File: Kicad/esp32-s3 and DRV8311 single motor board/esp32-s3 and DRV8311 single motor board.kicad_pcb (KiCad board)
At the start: 4 copper layers, 38.8 x 42.1 mm, 98 parts, among them J1 JST SH SM04B, J2 7 pin FPC 0.3mm, J3 Molex_PicoBlade_53048-0310 Ho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, J4 Conn_01x02_Pin, Q3 PMOS,Si7157DP, Q4 PMOS, SW1 SW_Push, SW2 SW_Push, U1 AP2112K-3.3, U2 DRV8311HRRWR, U4 BQ25060, U5 ESP32-S3, U6 74HC595, Y1 40mhz, 10ppm

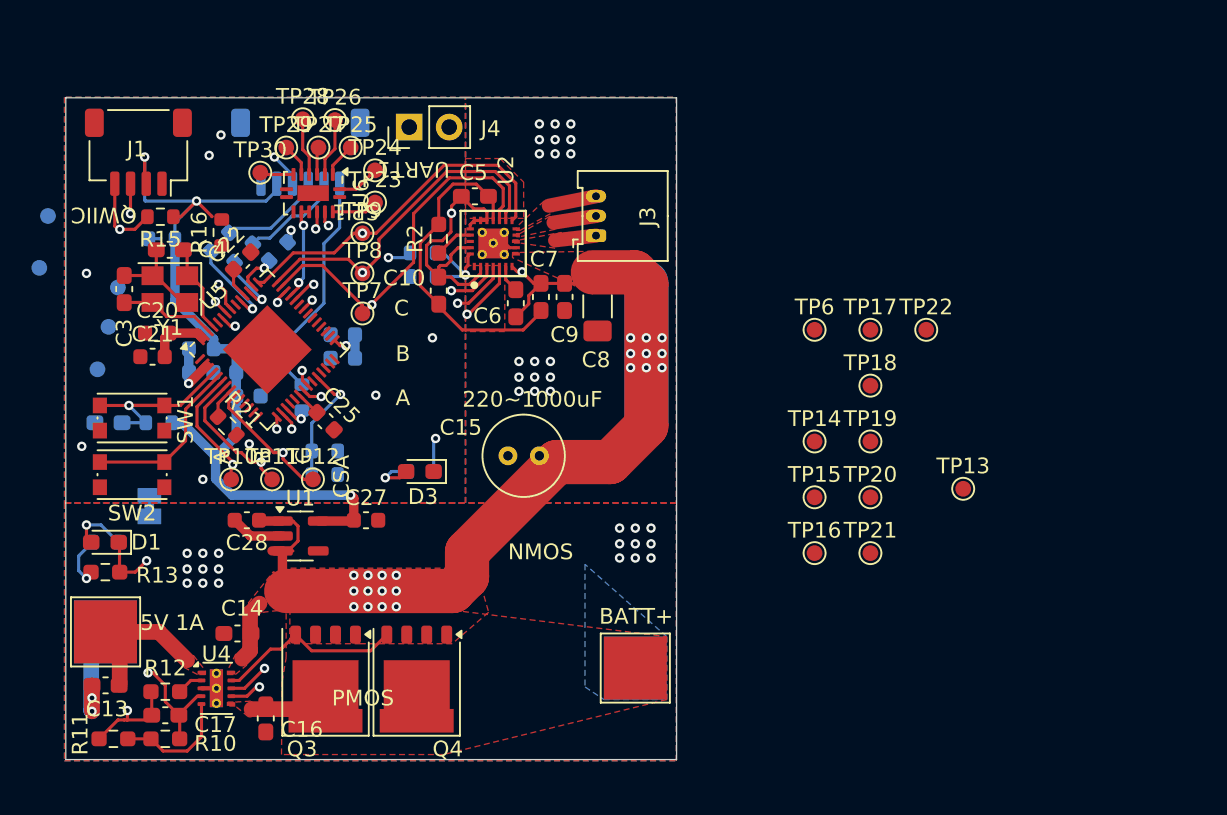
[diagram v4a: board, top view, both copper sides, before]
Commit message: Routing test pads & power
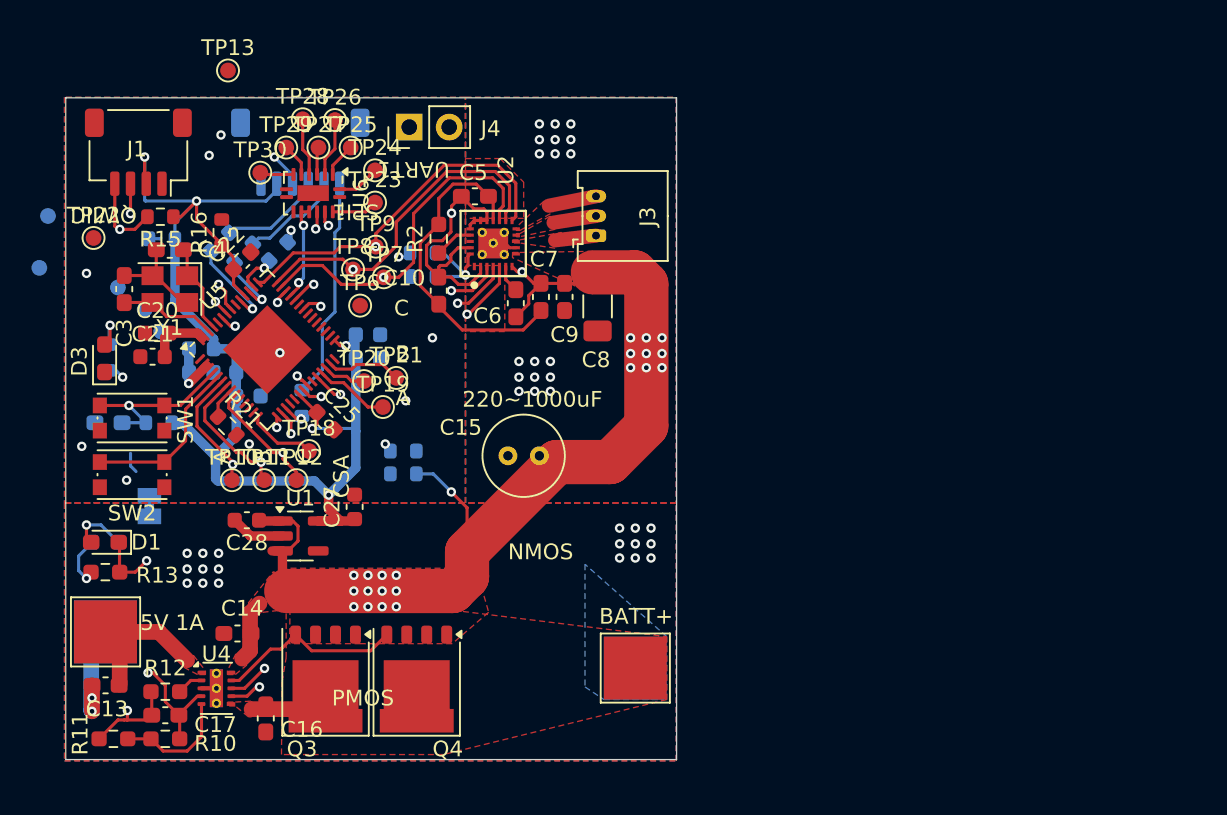
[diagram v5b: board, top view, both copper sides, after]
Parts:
- removed TP14, TP15, TP16, TP17: ~, TestPoint:TestPoint_Pad_D1.0mm
- moved TP13 53.8 mm to (133.0, 86.4)
- moved TP22 53.3 mm to (124.5, 97.0)
- moved TP18 35.9 mm to (138.2, 110.6)
- moved TP20 33.0 mm to (141.7, 106.2)
- moved TP21 32.1 mm to (143.7, 106.0)
- moved TP19 31.1 mm to (142.8, 107.8)
- moved TP6 28.9 mm to (141.4, 101.3)
- moved D3 21.3 mm to (125.2, 104.7), turned to 90 degrees
- moved R19 21.1 mm to (125.5, 104.7), turned to 90 degrees
- moved R17 5.00 mm to (144.2, 112.0)
- moved R18 5.00 mm to (144.2, 110.6)
- moved TP5 4.84 mm to (127.7, 101.6)
- moved TP1 3.36 mm to (128.8, 103.0)
- moved TP7 2.67 mm to (142.9, 99.5)
- moved C23 1.60 mm to (141.9, 103.2), turned to 0 degrees
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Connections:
- C28 pad 2: GND -> GNDPWR
- U1 pad 2: GND -> GNDPWR
- U2 pad 10: Net-(J3-Pin_3) -> Net-(J3-Pin_1)
- U2 pad 12: Net-(J3-Pin_1) -> Net-(J3-Pin_3)
- U5 pad 10: Net-(U5-GPIO5) -> unconnected-(U5-GPIO5-Pad10)
- U5 pad 11: Net-(U5-GPIO6) -> unconnected-(U5-GPIO6-Pad11)
- U5 pad 12: Net-(U5-GPIO7) -> unconnected-(U5-GPIO7-Pad12)
- U5 pad 13: Net-(U5-GPIO8) -> unconnected-(U5-GPIO8-Pad13)
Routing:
- net VDD: track 65.7 -> 83.4 mm, vias 4 -> 5
- net /MOTORPWR: track 126.1 -> 114.3 mm, vias 23 -> 24
- net /LED: track 3.19 -> 10.6 mm
- net Net-(U5-GPIO19/USB_D-): track 0.00 -> 4.83 mm
- net Net-(U5-GPIO21): track 0.00 -> 4.82 mm
- net Net-(U5-GPIO9): track 0.00 -> 4.40 mm
- net GNDPWR: track 9.07 -> 12.5 mm
- net GND: track 66.9 -> 63.5 mm, vias 10 -> 11
- net /1CSA-A: track 33.8 -> 36.9 mm
- net /1CSA-B: track 33.0 -> 35.8 mm
- net Net-(U5-GPIO20/USB_D+): track 0.00 -> 2.78 mm
- net /1CSA-C: track 30.4 -> 32.2 mm
- net unconnected-(U5-GPIO5-Pad10): track 0.00 -> 1.29 mm
- net /1C: track 29.4 -> 30.4 mm
- net /VBATT: track 7.82 -> 6.88 mm, vias 1 -> 2
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
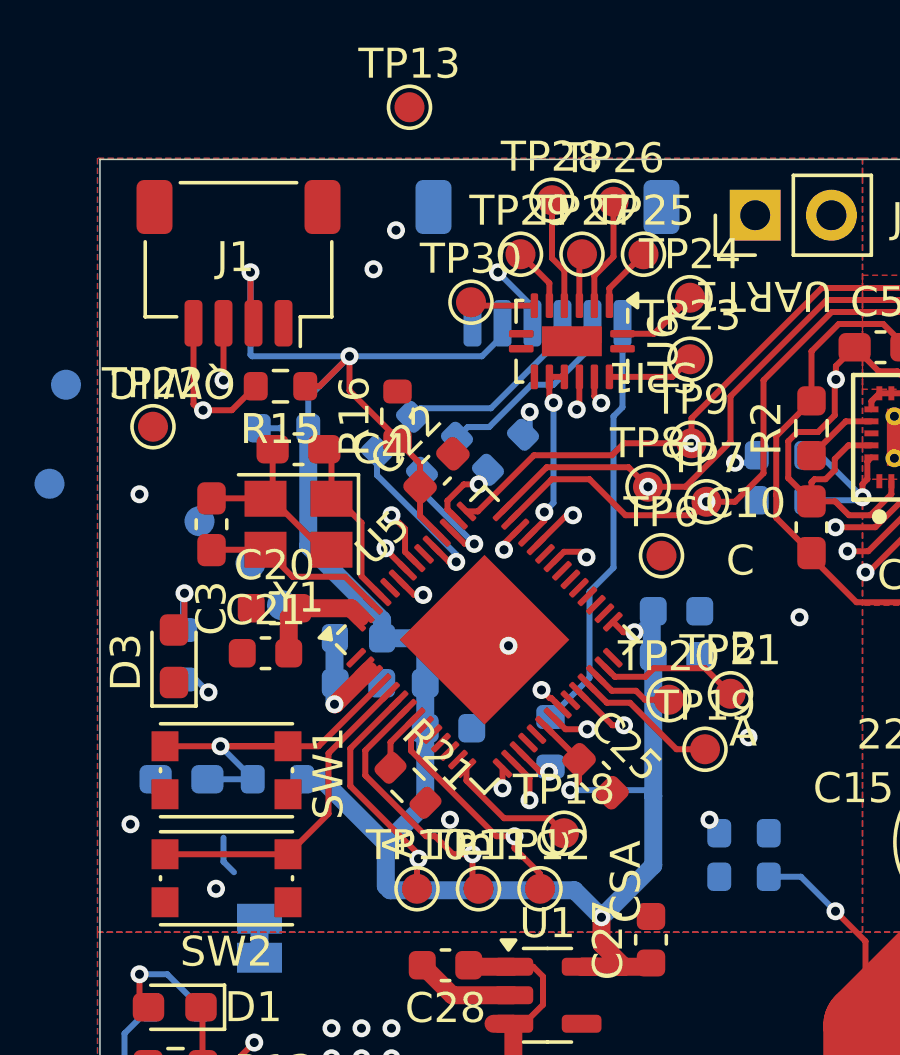
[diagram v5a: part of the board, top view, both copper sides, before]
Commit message: Added 7 pin FPC connector footprint
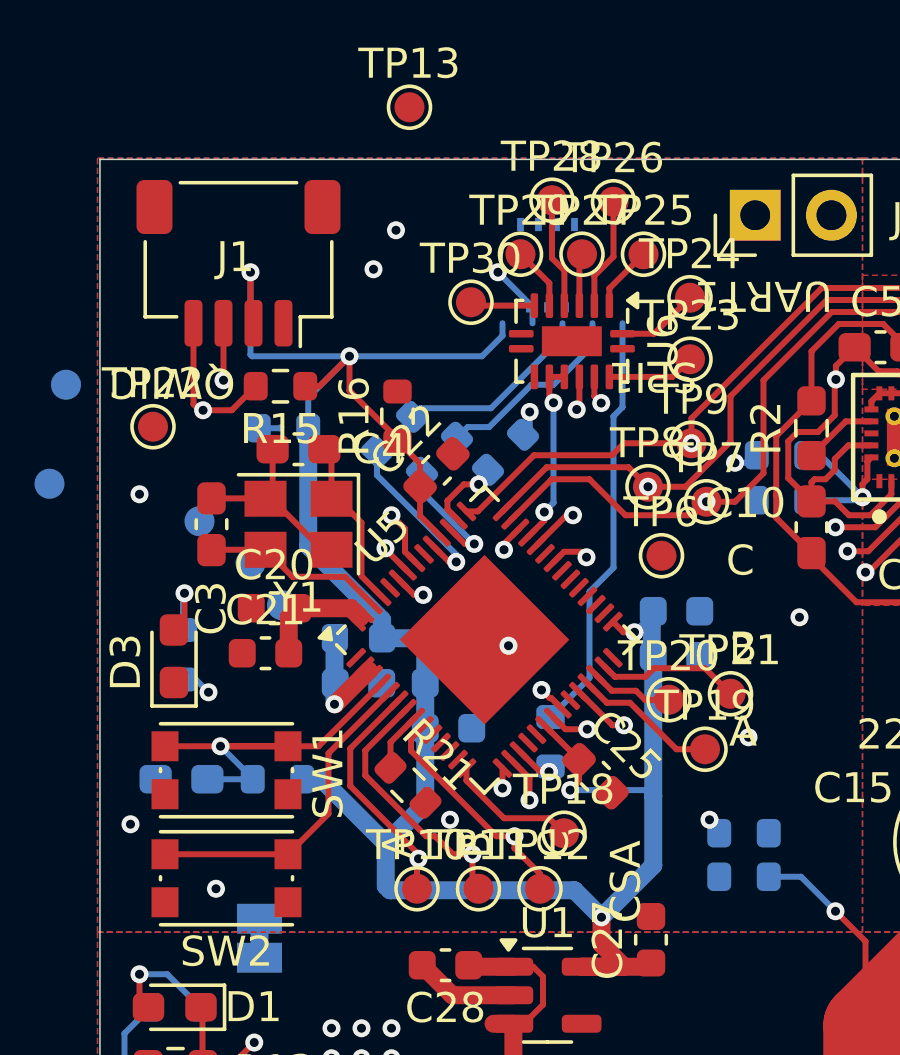
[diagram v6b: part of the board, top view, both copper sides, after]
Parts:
- J2: footprint Connector_JST:JST_SH_SM06B-SRSS-TB_1x06-1MP_P1.00mm_Horizontal -> custom_Interface_HID:fpc_7pin_0.3mm_connector Panasonic
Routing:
- net unconnected-(U5-GPIO5-Pad10): track 1.29 -> 0.00 mm

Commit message: Finished routing everything
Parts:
- removed J4: Conn_01x02_Pin, Connector_PinHeader_2.54mm:PinHeader_1x02_P2.54mm_Vertical
- removed TP13, TP2, TP3, TP4, TP5: TestPoint, TestPoint:TestPoint_Pad_D1.0mm
- added TP14: TestPoint, TestPoint:TestPoint_Pad_D1.0mm, F.Cu at (143.2, 111.5)
- added TP15: TestPoint, TestPoint:TestPoint_Pad_D1.0mm, F.Cu at (141.2, 111.5)
- R15: moved to B.Cu
- moved TP1 8.20 mm to (136.9, 102.8)
- moved TP22 4.03 mm to (124.0, 101.0)
- moved TP29 2.39 mm to (134.6, 92.3)
- moved TP28 2.02 mm to (136.9, 91.3)
- moved TP25 1.88 mm to (141.7, 93.0)
- moved TP26 1.86 mm to (140.6, 91.2)
- moved J1 1.86 mm to (127.2, 93.5)
- moved TP24 1.78 mm to (143.3, 94.2)
- moved TP30 1.53 mm to (134.8, 94.4)
- moved TP23 1.01 mm to (141.8, 95.7)
- moved J2 1.01 mm to (138.6, 91.9)
- moved TP27 1.00 mm to (138.8, 92.3)
- moved U6 1.00 mm to (138.4, 95.2)
- moved C4 0.50 mm to (128.8, 97.8)
- moved Y1 0.40 mm to (128.9, 100.2)
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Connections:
- J2 pad 1: GND -> VDD
- J2 pad 2: VDD -> /SCK1
- J2 pad 3: /SCK1 -> GND
- J2 pad 5: /MOSI1 -> /CS1
- J2 pad 6: /CS1 -> /MOSI1
- J2 pad 7: (no net) -> GND
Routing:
- net VDD: track 83.4 -> 100.1 mm, vias 5 -> 6
- net Net-(U5-GPIO46): track 0.00 -> 14.6 mm
- net /CS1: track 14.1 -> 26.1 mm, vias 0 -> 1
- net Net-(U5-SPICLK_P): track 0.00 -> 4.31 mm
- net /CS0: track 0.00 -> 4.21 mm, vias 0 -> 1
- net GND: track 63.5 -> 67.0 mm, vias 11 -> 13
- net /UART0_RX: track 20.5 -> 17.5 mm, vias 1 -> 2
- net /UART0_TX: track 19.6 -> 22.3 mm, vias 1 -> 2
- net Net-(U6-QG): track 2.11 -> 4.46 mm
- net Net-(U5-GPIO0): track 10.9 -> 9.02 mm
- net /VBATT: track 6.88 -> 8.46 mm
- net Net-(U5-GPIO33): track 6.73 -> 5.57 mm
- net Net-(U5-GPIO35): track 8.49 -> 7.49 mm
- net Net-(U5-GPIO34): track 6.24 -> 5.24 mm
- net /SDA1: track 20.9 -> 21.8 mm
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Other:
- board size 38.8 x 42.1 mm -> 38.8 x 40.3 mm

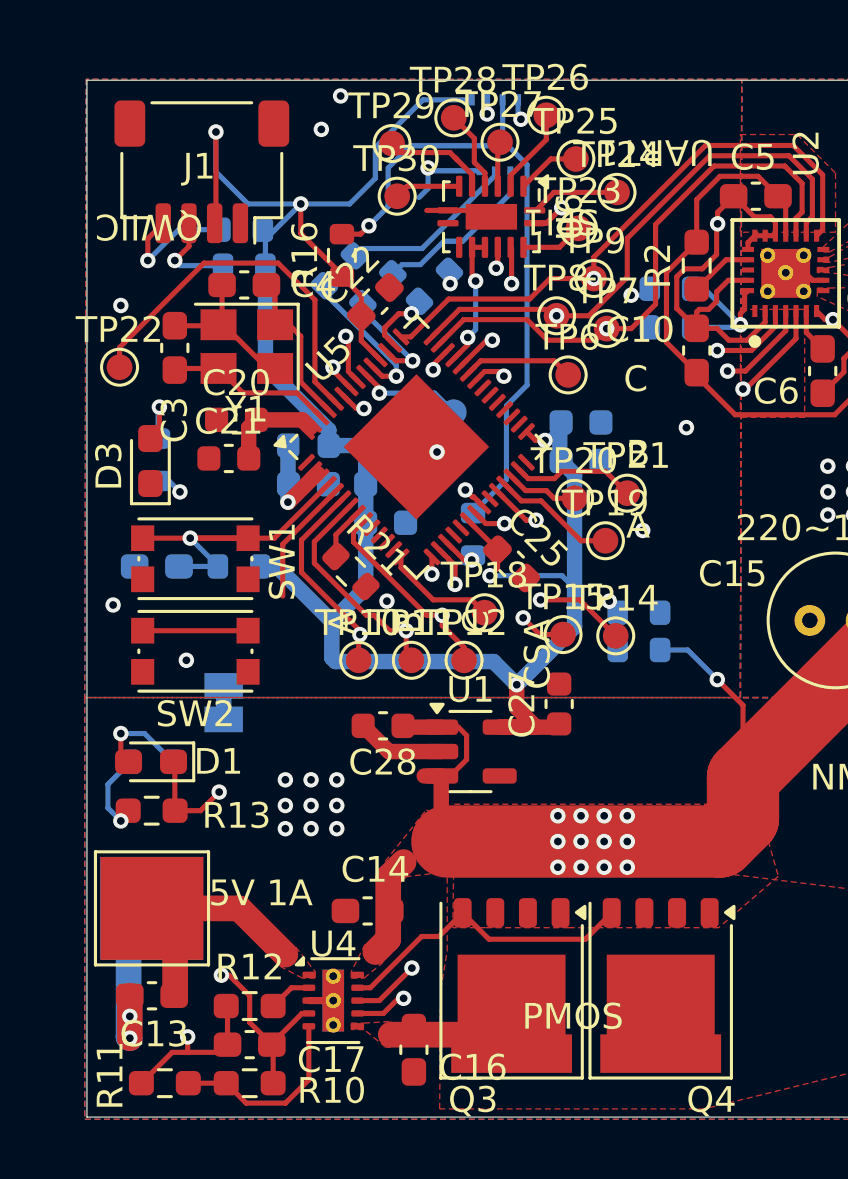
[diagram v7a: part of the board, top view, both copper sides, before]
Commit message: Fixed DRC errors
I still have to fix all the silkscreen issues
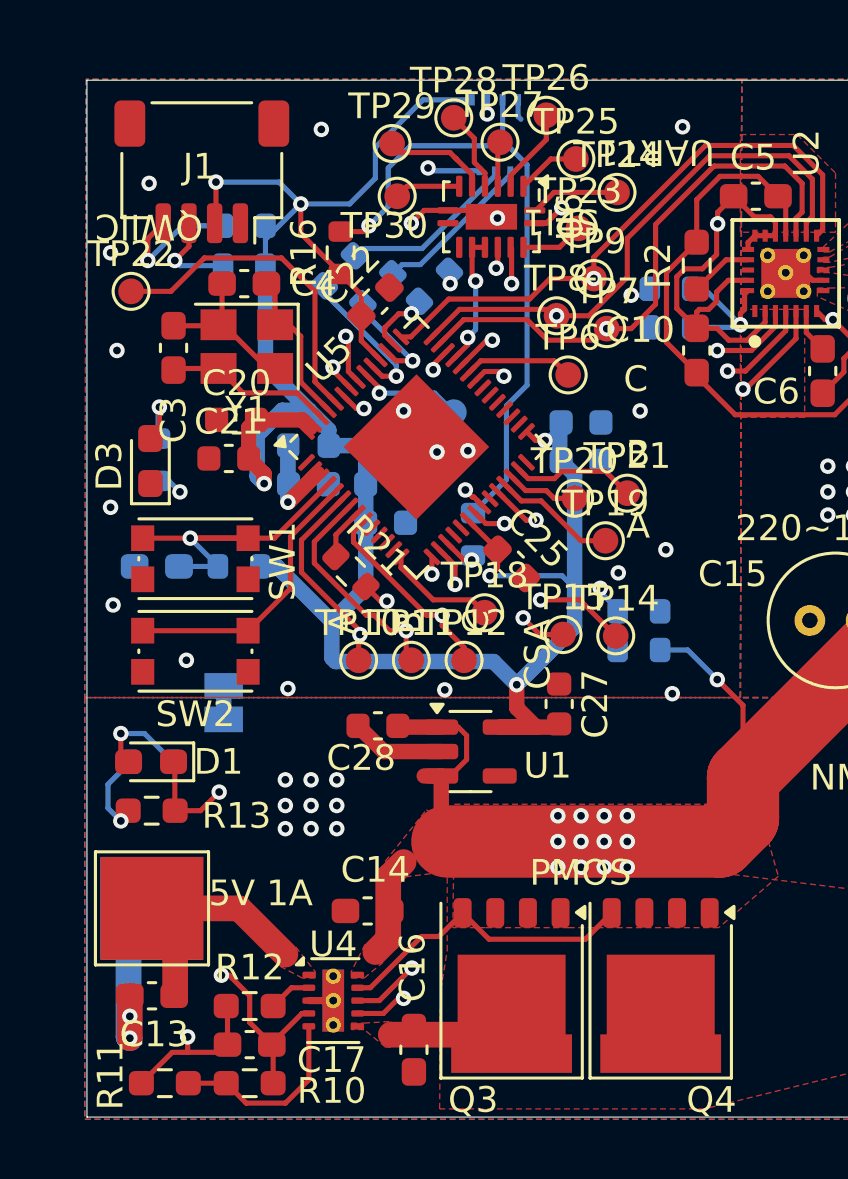
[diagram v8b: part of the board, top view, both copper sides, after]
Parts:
- moved TP22 2.98 mm to (124.4, 98.1)
- moved C28 0.20 mm to (134.0, 115.0)
- moved R15 0.18 mm to (128.8, 95.5)
- moved R16 0.11 mm to (132.6, 96.6)
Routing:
- net /UART0_TX: track 22.3 -> 19.9 mm
- net VDD: track 100.1 -> 102.3 mm, vias 6 -> 7
- net GND: track 67.0 -> 69.0 mm, vias 13 -> 23
- net Net-(U5-GPIO0): track 9.02 -> 10.9 mm
- net Net-(U5-GPIO46): track 14.6 -> 12.9 mm
- net /SCK1: track 8.69 -> 7.40 mm
